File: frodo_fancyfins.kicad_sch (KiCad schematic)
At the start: 2 parts, among them J1 Molex MicroFit 2x3, J2 Molex MicroFit 2x3

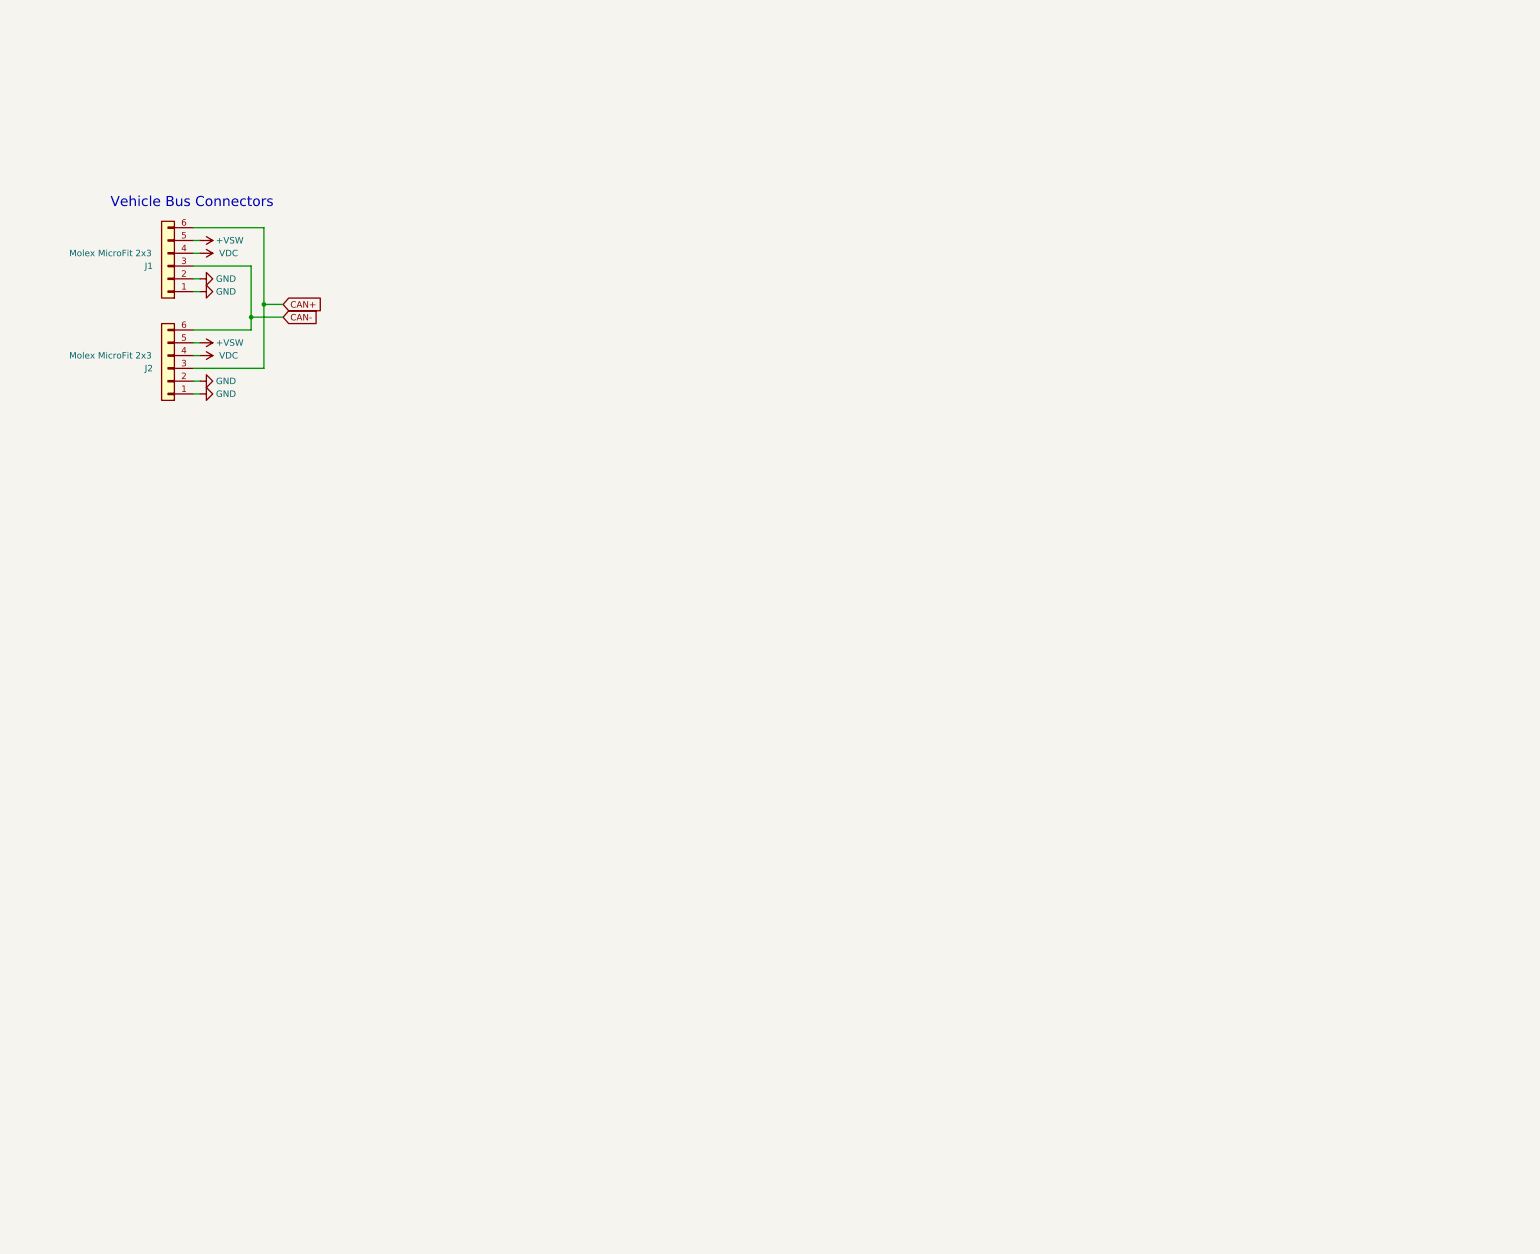
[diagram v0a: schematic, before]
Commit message: Add INA826, antenna symbol and antenna footprint
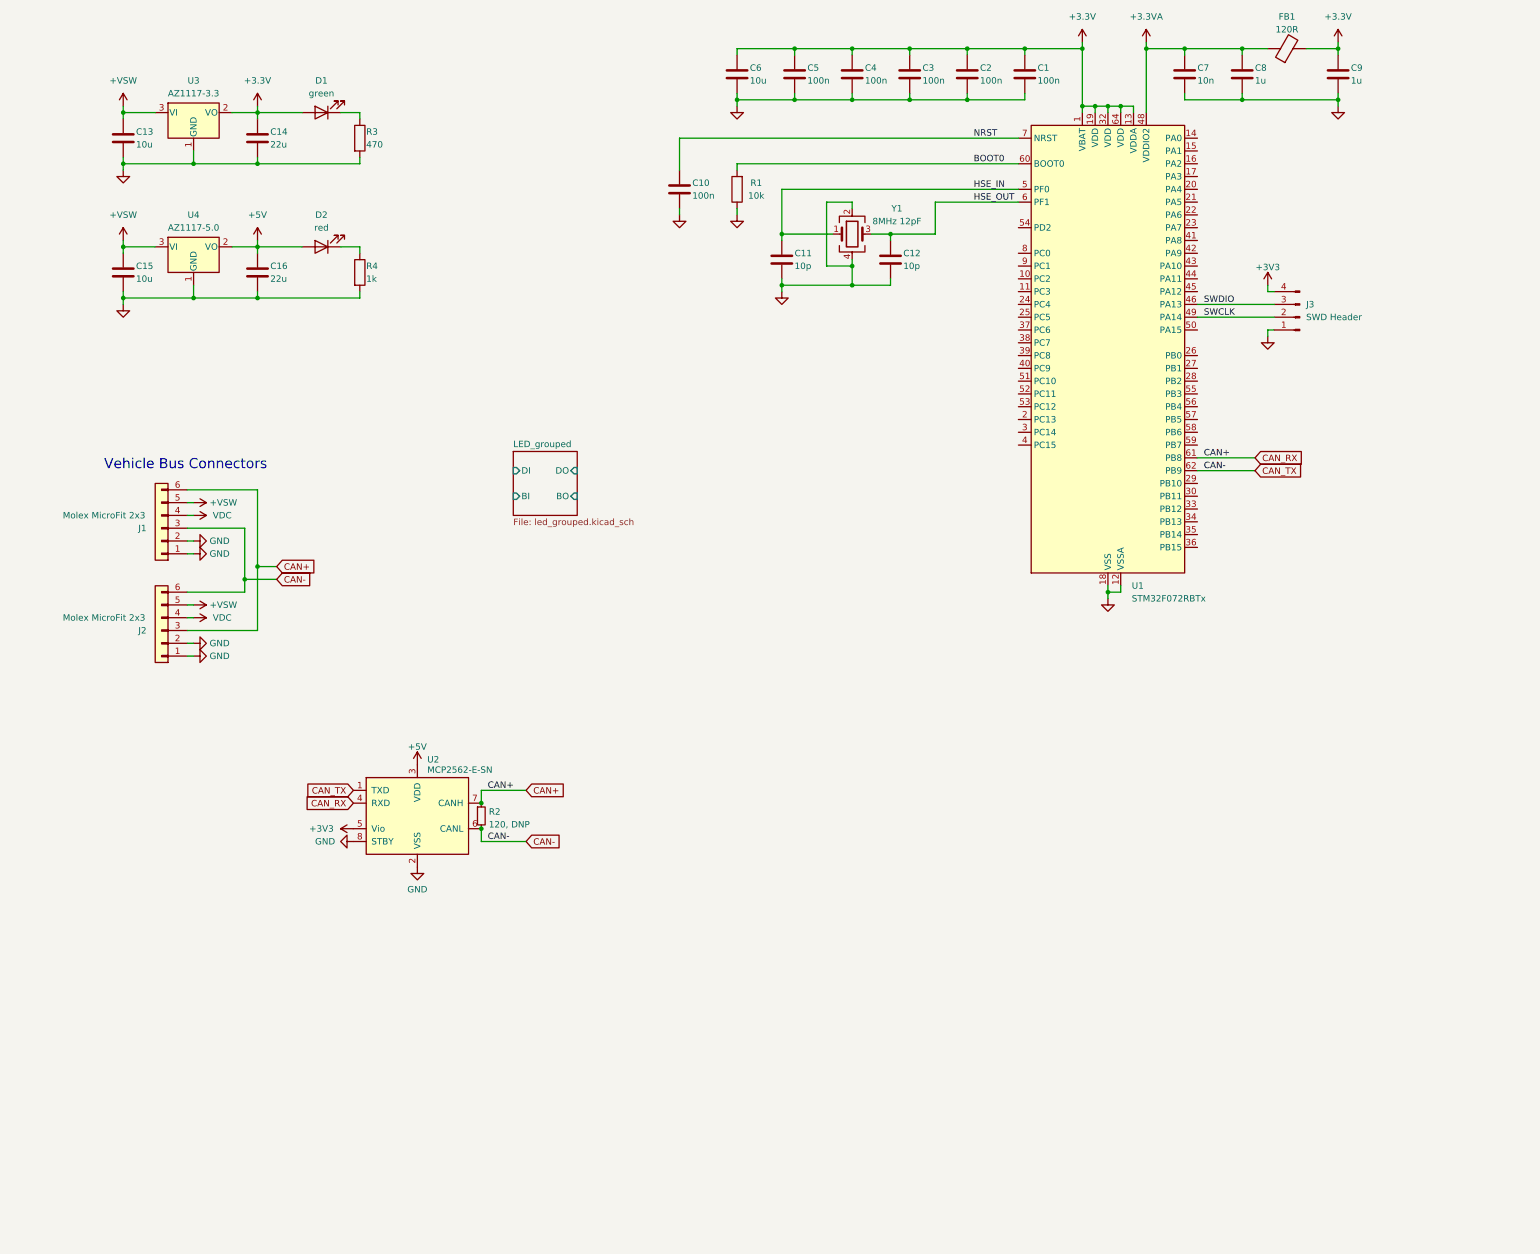
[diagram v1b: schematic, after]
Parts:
- added C1, C10, C2, C3, C4, C5: 100n, symbol Device:C
- added C11, C12: 10p, symbol Device:C
- added C13, C15, C6: 10u, symbol Device:C
- added C14, C16: 22u, symbol Device:C
- added C7: 10n, symbol Device:C
- added C8, C9: 1u, symbol Device:C
- added D1: green, symbol Device:LED
- added D2: red, symbol Device:LED
- added FB1: 120R, symbol Device:FerriteBead
- added J3: SWD Header, symbol Connector:Conn_01x04_Pin
- added R1: 10k, symbol Device:R
- added R2: 120, DNP, Resistor_SMD:R_0603_1608Metric, symbol Device:R_Small
- added R3: 470, symbol Device:R
- added R4: 1k, symbol Device:R
- added U1: STM32F072RBTx, Package_QFP:LQFP-64_10x10mm_P0.5mm, symbol MCU_ST_STM32F0:STM32F072RBTx
- added U2: MCP2562-E-SN, Package_SO:SOIC-8_3.9x4.9mm_P1.27mm, symbol Interface_CAN_LIN:MCP2562-E-SN
- added U3: AZ1117-3.3, symbol Regulator_Linear:AZ1117-3.3
- added U4: AZ1117-5.0, symbol Regulator_Linear:AZ1117-5.0
- added Y1: 8MHz 12pF, symbol Device:Crystal_GND24
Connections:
- net +VSW: now also C13.1, C15.1, U3.3 (VI), U4.3 (VI)
- net CAN+: now also R2.1, U1.61 (PB8), U2.4 (RXD), U2.7 (CANH)
- net CAN-: now also R2.2, U1.62 (PB9), U2.1 (TXD), U2.6 (CANL)
- net GND: now also C1.2, C10.2, C11.2, C12.2, C13.2, C14.2, C15.2, C16.2, C2.2, C3.2, C4.2, C5.2, C6.2, C7.2, C8.2, C9.2, J3.1 (Pin_1), R1.1, R3.2, R4.2, U1.12 (VSSA), U1.18 (VSS), U1.31 (VSS), U1.47 (VSS), U1.63 (VSS), U2.2 (VSS), U2.8 (STBY), U3.1 (GND), U4.1 (GND), Y1.2, Y1.4
- new net: D2.1 (K), R4.1
- new net: D1.1 (K), R3.1
- new net +3.3V: C1.1, C14.1, C2.1, C3.1, C4.1, C5.1, C6.1, C9.1, D1.2 (A), FB1.2, U1.1 (VBAT), U1.13 (VDDA), U1.19 (VDD), U1.32 (VDD), U1.64 (VDD), U3.2 (VO)
- new net +3.3VA: C7.1, C8.1, FB1.1, U1.48 (VDDIO2)
- new net +3V3: J3.4 (Pin_4), U2.5 (Vio)
- new net +5V: C16.1, D2.2 (A), U2.3 (VDD), U4.2 (VO)
- new net BOOT0: R1.2, U1.60 (BOOT0)
- new net HSE_IN: C11.1, U1.5 (PF0), Y1.1
- new net HSE_OUT: C12.1, U1.6 (PF1), Y1.3
- new net NRST: C10.1, U1.7 (NRST)
- new net SWCLK: J3.2 (Pin_2), U1.49 (PA14)
- new net SWDIO: J3.3 (Pin_3), U1.46 (PA13)
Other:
- added sheet LED_grouped (led_grouped.kicad_sch)
- moved on the sheet: J1, J2

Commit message: Add RGB LED schematics
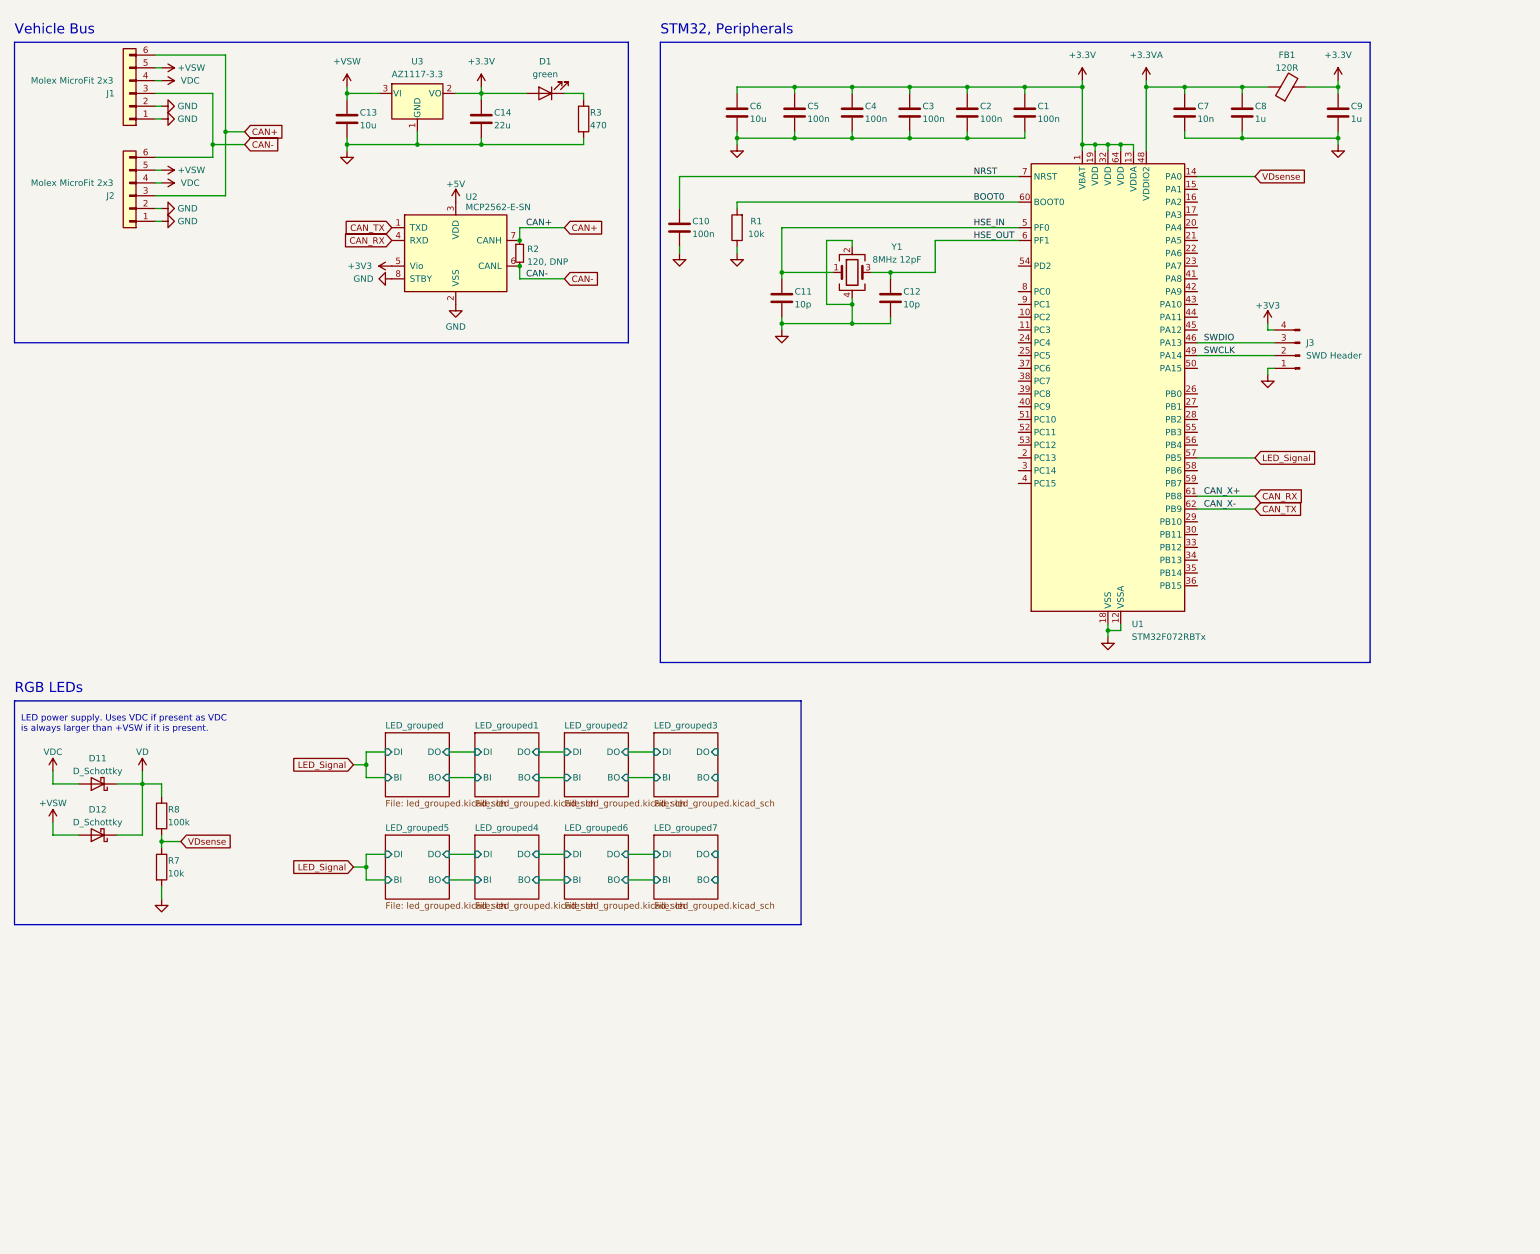
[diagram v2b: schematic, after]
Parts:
- removed C15: 10u, symbol Device:C
- removed C16: 22u, symbol Device:C
- removed D2: red, symbol Device:LED
- removed R4: 1k, symbol Device:R
- removed U4: AZ1117-5.0, symbol Regulator_Linear:AZ1117-5.0
- added D11, D12: D_Schottky, symbol Device:D_Schottky
- added R7: 10k, symbol Device:R
- added R8: 100k, symbol Device:R
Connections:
- net +VSW: now also D12.2 (A)
- net CAN+: no longer U1.61 (PB8), U2.4 (RXD)
- net CAN-: no longer U1.62 (PB9), U2.1 (TXD)
- net GND: now also R7.2
- net VDC: now also D11.2 (A)
- net VDsense: now reaches U1.14 (PA0)
- net VDsense: now also R7.1, R8.2
- net LED_Signal: now reaches U1.57 (PB5)
- new net CAN_RX: U1.61 (PB8), U2.4 (RXD)
- new net CAN_TX: U1.62 (PB9), U2.1 (TXD)
- new net VD: D11.1 (K), D12.1 (K), R8.1
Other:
- added sheet LED_grouped1 (led_grouped.kicad_sch)
- added sheet LED_grouped2 (led_grouped.kicad_sch)
- added sheet LED_grouped3 (led_grouped.kicad_sch)
- added sheet LED_grouped4 (led_grouped.kicad_sch)
- added sheet LED_grouped5 (led_grouped.kicad_sch)
- added sheet LED_grouped6 (led_grouped.kicad_sch)
- added sheet LED_grouped7 (led_grouped.kicad_sch)
- note added: "LED power supply. Uses VDC if present as VDC is always larger than +VSW if it is present."
- note added: "RGB LEDs"
- note added: "STM32, Peripherals"
- note added: "Vehicle Bus"
- note removed: "Vehicle Bus Connectors"
- moved on the sheet: C1, C10, C11, C12, C13, C14, C2, C3, C4, C5, C6, C7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

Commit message: Schematics cleanup
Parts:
- removed J3: SWD Header, symbol Connector:Conn_01x04_Pin
- added J4: SWD Header, Connector_PinHeader_2.54mm:PinHeader_1x04_P2.54mm_Vertical, symbol Connector_Generic:Conn_01x04
- added R4: 1k, symbol Device:R
- C11, C12: value 10p -> 15p
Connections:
- net +3V3: now also J4.1 (Pin_1)
- net GND: now also J4.4 (Pin_4)
- net SWCLK: now also J4.3 (Pin_3)
- net SWDIO: now also J4.2 (Pin_2)
- net HSE_IN: no longer names the net of C11.1, Y1.1
- net HSE_IN: now also R4.2; no longer U1.5 (PF0)
- net HSE_OUT renamed OSC_OUT
- new net OSC_IN: R4.1, U1.5 (PF0)
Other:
- note added: "3V3 Regulator"
- note added: "CAN Tranceiver"
- note added: "MCU"
- note added: "Refer to AN2867 TODO: Check the component values after selecting the specific crystal."
- note removed: "STM32, Peripherals"
- moved on the sheet: C1, C10, C11, C12, C13, C14, C2, C3, C4, C5, C6, C7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
